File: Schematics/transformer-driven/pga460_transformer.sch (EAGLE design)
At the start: 59 parts, among them IC1 PGA460TPWQ1, IC2 PGA460TPWQ1, IC3 PGA460TPWQ1, T1 B78416A2232A003, T2 B78416A2232A003, T3 B78416A2232A003

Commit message: change connector package
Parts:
- renumbered J1 to MCP2515
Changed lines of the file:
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@@
 <part name="5V/GND" library="con-lsta" library_urn="urn:adsk.eagle:library:161" deviceset="FE05-2" device="" package3d_urn="urn:adsk.eagle:package:8170/1"/>
 <part name="POWER" library="SparkFun-Connectors" deviceset="CONN_02" device=""/>
-<part name="J1" library="SparkFun-Connectors" deviceset="CONN_07" device=""/>
+<part name="MCP2515" library="SparkFun-Connectors" deviceset="CONN_07" device=""/>
 </parts>
 <sheets>
@@
 <attribute name="NAME" x="210.82" y="-131.572" size="1.778" layer="95" font="vector"/>
 </instance>
-<instance part="J1" gate="J1" x="241.3" y="-208.28" smashed="yes">
+<instance part="MCP2515" gate="J1" x="241.3" y="-208.28" smashed="yes">
 <attribute name="VALUE" x="236.22" y="-218.186" size="1.778" layer="96" font="vector"/>
 <attribute name="NAME" x="236.22" y="-195.072" size="1.778" layer="95" font="vector"/>
@@
 <wire x1="246.38" y1="-210.82" x2="251.46" y2="-210.82" width="0.1524" layer="91"/>
 <label x="251.46" y="-210.82" size="1.778" layer="95"/>
-<pinref part="J1" gate="J1" pin="2"/>
+<pinref part="MCP2515" gate="J1" pin="2"/>
 <junction x="246.38" y="-210.82"/>
 </segment>
@@
 <wire x1="246.38" y1="-213.36" x2="251.46" y2="-213.36" width="0.1524" layer="91"/>
 <label x="251.46" y="-213.36" size="1.778" layer="95"/>
-<pinref part="J1" gate="J1" pin="1"/>
+<pinref part="MCP2515" gate="J1" pin="1"/>
 <junction x="246.38" y="-213.36"/>
 </segment>
@@
 <wire x1="246.38" y1="-200.66" x2="251.46" y2="-200.66" width="0.1524" layer="91"/>
 <label x="251.46" y="-200.66" size="1.778" layer="95"/>
-<pinref part="J1" gate="J1" pin="6"/>
+<pinref part="MCP2515" gate="J1" pin="6"/>
 <junction x="246.38" y="-200.66"/>
 </segment>
@@
 <wire x1="246.38" y1="-198.12" x2="251.46" y2="-198.12" width="0.1524" layer="91"/>
 <label x="251.46" y="-198.12" size="1.778" layer="95"/>
-<pinref part="J1" gate="J1" pin="7"/>
+<pinref part="MCP2515" gate="J1" pin="7"/>
 <junction x="246.38" y="-198.12"/>
 </segment>
@@
 <wire x1="246.38" y1="-203.2" x2="251.46" y2="-203.2" width="0.1524" layer="91"/>
 <label x="251.46" y="-203.2" size="1.778" layer="95"/>
-<pinref part="J1" gate="J1" pin="5"/>
+<pinref part="MCP2515" gate="J1" pin="5"/>
 <junction x="246.38" y="-203.2"/>
 </segment>
@@
 <wire x1="246.38" y1="-205.74" x2="251.46" y2="-205.74" width="0.1524" layer="91"/>
 <label x="251.46" y="-205.74" size="1.778" layer="95"/>
-<pinref part="J1" gate="J1" pin="4"/>
+<pinref part="MCP2515" gate="J1" pin="4"/>
 <junction x="246.38" y="-205.74"/>
 </segment>
@@
 <wire x1="246.38" y1="-208.28" x2="251.46" y2="-208.28" width="0.1524" layer="91"/>
 <label x="251.46" y="-208.28" size="1.778" layer="95"/>
-<pinref part="J1" gate="J1" pin="3"/>
+<pinref part="MCP2515" gate="J1" pin="3"/>
 <junction x="246.38" y="-208.28"/>
 </segment>

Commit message: change pga460
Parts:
- removed IC1, IC2, IC3: PGA460TPWQ1, PGA460TPWQ1:PGA460TPWQ1
- added U1, U2, U4: PGA460, texas:PGA460
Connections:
- net AVDD1: now also U4.AVDD; no longer IC1.AVDD
- net AVDD2: now also U1.AVDD; no longer IC2.AVDD
- net AVDD3: now also U2.AVDD; no longer IC3.AVDD
- net GND: now also U1.GND, U1.GND1, U1.GNDP, U2.GND, U2.GND1, U2.GNDP, U4.GND, U4.GND1, U4.GNDP; no longer IC1.GNDP, IC1.GND_1, IC1.GND_2, IC2.GNDP, IC2.GND_1, IC2.GND_2, IC3.GNDP, IC3.GND_1, IC3.GND_2
- net INN_1: now also U4.INN; no longer IC1.INN
- net INN_2: now also U1.INN; no longer IC2.INN
- net INN_3: now also U2.INN; no longer IC3.INN
- net INP_1: now also U4.INP; no longer IC1.INP
- net INP_2: now also U1.INP; no longer IC2.INP
- net INP_3: now also U2.INP; no longer IC3.INP
- net IOREG1: now also U4.IOREG; no longer IC1.IOREG
- net IOREG2: now also U1.IOREG; no longer IC2.IOREG
- net IOREG3: now also U2.IOREG; no longer IC3.IOREG
- net OUTA_1: now also U4.OUTA; no longer IC1.OUTA
- net OUTA_2: now also U1.OUTA; no longer IC2.OUTA
- net OUTA_3: now also U2.OUTA; no longer IC3.OUTA
- net OUTB_1: now also U4.OUTB; no longer IC1.OUTB
- net OUTB_2: now also U1.OUTB; no longer IC2.OUTB
- net OUTB_3: now also U2.OUTB; no longer IC3.OUTB
- net RX1: now also U4.TXD; no longer IC1.TXD
- net RX2: now also U1.TXD; no longer IC2.TXD
- net RX3: now also U2.TXD; no longer IC3.TXD
- net SCLK1: now also U4.SCLK; no longer IC1.SCLK
- net SCLK2: now also U1.SCLK; no longer IC2.SCLK
- net SCLK3: now also U2.SCLK; no longer IC3.SCLK
- net TEST1: no longer IC1.TEST
- net TEST2: no longer IC2.TEST
- net TEST3: no longer IC3.TEST
- net TX1: now also U4.RXD; no longer IC1.RXD
- net TX2: now also U1.RXD; no longer IC2.RXD
- net TX3: now also U2.RXD; no longer IC3.RXD
- net VIN: now also U1.VPWR, U2.VPWR, U4.VPWR; no longer IC1.VPWR, IC2.VPWR, IC3.VPWR

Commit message: Revert "change pga460"
This reverts commit 11281d79b47b0006704001165f10d30d9cd033b8
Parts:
- removed U1, U2, U4: PGA460, texas:PGA460
- added IC1, IC2, IC3: PGA460TPWQ1, PGA460TPWQ1:PGA460TPWQ1
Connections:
- net AVDD1: now also IC1.AVDD; no longer U4.AVDD
- net AVDD2: now also IC2.AVDD; no longer U1.AVDD
- net AVDD3: now also IC3.AVDD; no longer U2.AVDD
- net GND: now also IC1.GNDP, IC1.GND_1, IC1.GND_2, IC2.GNDP, IC2.GND_1, IC2.GND_2, IC3.GNDP, IC3.GND_1, IC3.GND_2; no longer U1.GND, U1.GND1, U1.GNDP, U2.GND, U2.GND1, U2.GNDP, U4.GND, U4.GND1, U4.GNDP
- net INN_1: now also IC1.INN; no longer U4.INN
- net INN_2: now also IC2.INN; no longer U1.INN
- net INN_3: now also IC3.INN; no longer U2.INN
- net INP_1: now also IC1.INP; no longer U4.INP
- net INP_2: now also IC2.INP; no longer U1.INP
- net INP_3: now also IC3.INP; no longer U2.INP
- net IOREG1: now also IC1.IOREG; no longer U4.IOREG
- net IOREG2: now also IC2.IOREG; no longer U1.IOREG
- net IOREG3: now also IC3.IOREG; no longer U2.IOREG
- net OUTA_1: now also IC1.OUTA; no longer U4.OUTA
- net OUTA_2: now also IC2.OUTA; no longer U1.OUTA
- net OUTA_3: now also IC3.OUTA; no longer U2.OUTA
- net OUTB_1: now also IC1.OUTB; no longer U4.OUTB
- net OUTB_2: now also IC2.OUTB; no longer U1.OUTB
- net OUTB_3: now also IC3.OUTB; no longer U2.OUTB
- net RX1: now also IC1.TXD; no longer U4.TXD
- net RX2: now also IC2.TXD; no longer U1.TXD
- net RX3: now also IC3.TXD; no longer U2.TXD
- net SCLK1: now also IC1.SCLK; no longer U4.SCLK
- net SCLK2: now also IC2.SCLK; no longer U1.SCLK
- net SCLK3: now also IC3.SCLK; no longer U2.SCLK
- net TEST1: now also IC1.TEST
- net TEST2: now also IC2.TEST
- net TEST3: now also IC3.TEST
- net TX1: now also IC1.RXD; no longer U4.RXD
- net TX2: now also IC2.RXD; no longer U1.RXD
- net TX3: now also IC3.RXD; no longer U2.RXD
- net VIN: now also IC1.VPWR, IC2.VPWR, IC3.VPWR; no longer U1.VPWR, U2.VPWR, U4.VPWR

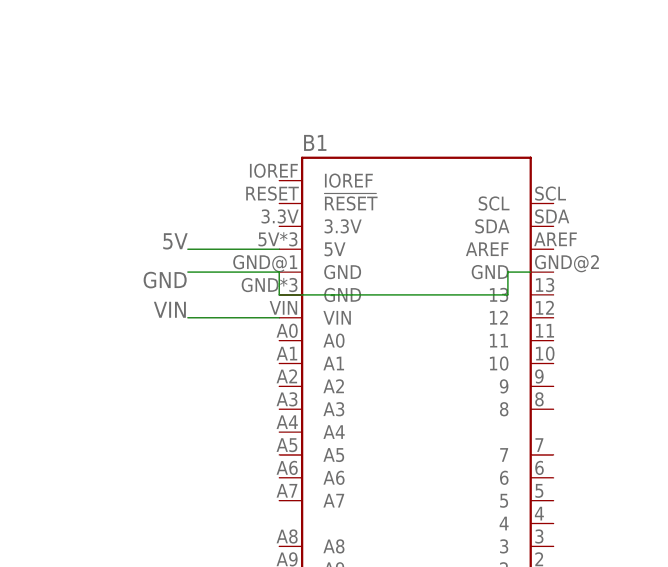
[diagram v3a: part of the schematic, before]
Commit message: Prevent smaller gaps between tracks
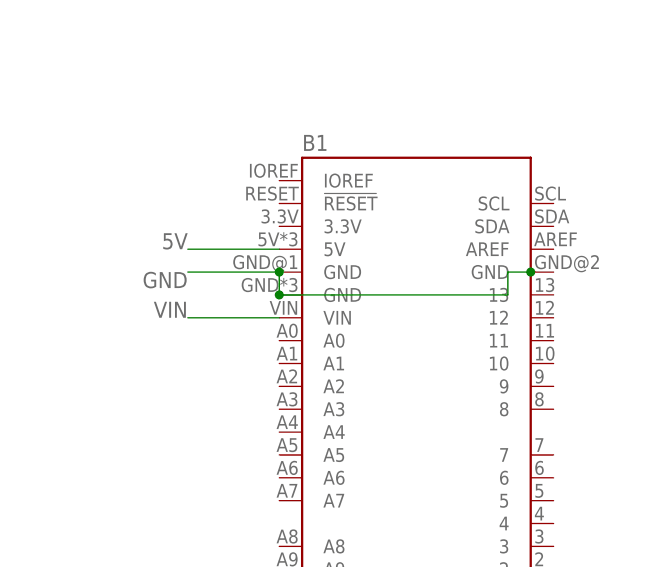
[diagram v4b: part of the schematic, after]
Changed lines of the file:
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@@
 <wire x1="320.04" y1="-71.12" x2="320.04" y2="-68.58" width="0.1524" layer="91"/>
 <wire x1="320.04" y1="-68.58" x2="322.58" y2="-68.58" width="0.1524" layer="91"/>
+<junction x="294.64" y="-68.58"/>
+<junction x="294.64" y="-71.12"/>
+<junction x="322.58" y="-68.58"/>
 </segment>
 <segment>
